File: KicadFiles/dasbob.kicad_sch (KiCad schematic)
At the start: 64 parts, among them J1 TRRS LEFT, J2 TRRS LEFT, SW1 SW_Push, SW10 SW_Push, SW11 SW_Push, SW12 SW_Push, SW13 SW_Push, SW14 SW_Push, SW15 SW_Push, SW16 SW_Push, SW17 SW_Push, SW18 SW_Push, SW19 SW_Push, SW2 SW_Push, SW20 SW_Push, SW21 SW_Push, SW22 SW_Push, SW23 SW_Push, SW24 SW_Push, SW25 SW_Push, SW26 SW_Push, SW27 SW_Push, SW28 SW_Push, SW29 SW_Push, SW3 SW_Push, SW30 SW_Push, SW31 SW_Push, SW32 SW_Push, SW33 SW_Push, SW34 SW_Push, SW35 SW_Push, SW36 SW_Push, SW4 SW_Push, SW5 SW_Push, SW6 SW_Push, SW7 SW_Push, SW8 SW_Push, SW9 SW_Push, U1 Elite-C RIGHT, U2 Elite-C LEFT, U3 OLED1, U4 OLED2

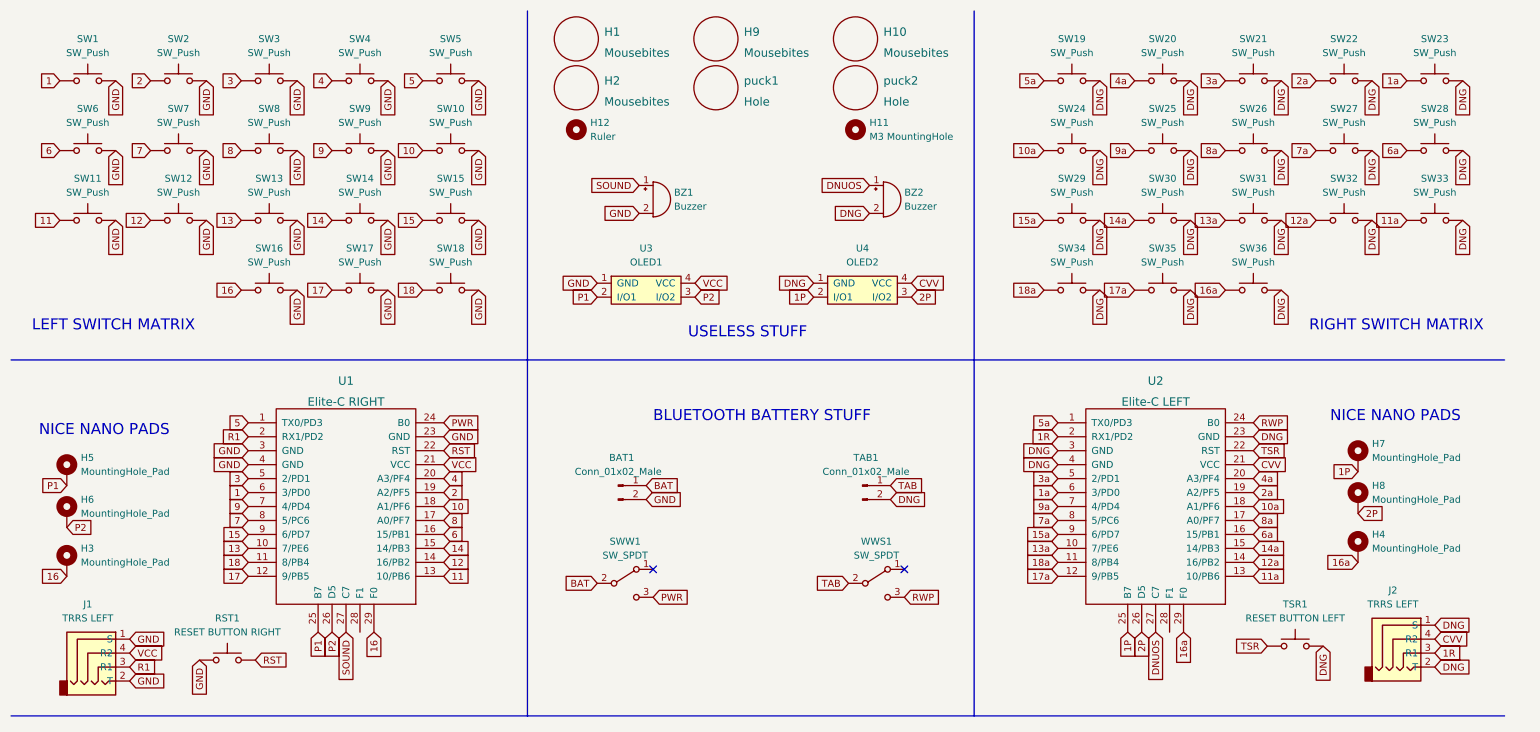
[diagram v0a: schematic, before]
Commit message: routed the oled to the wrong pins because im a ducking idiot now i fixed it
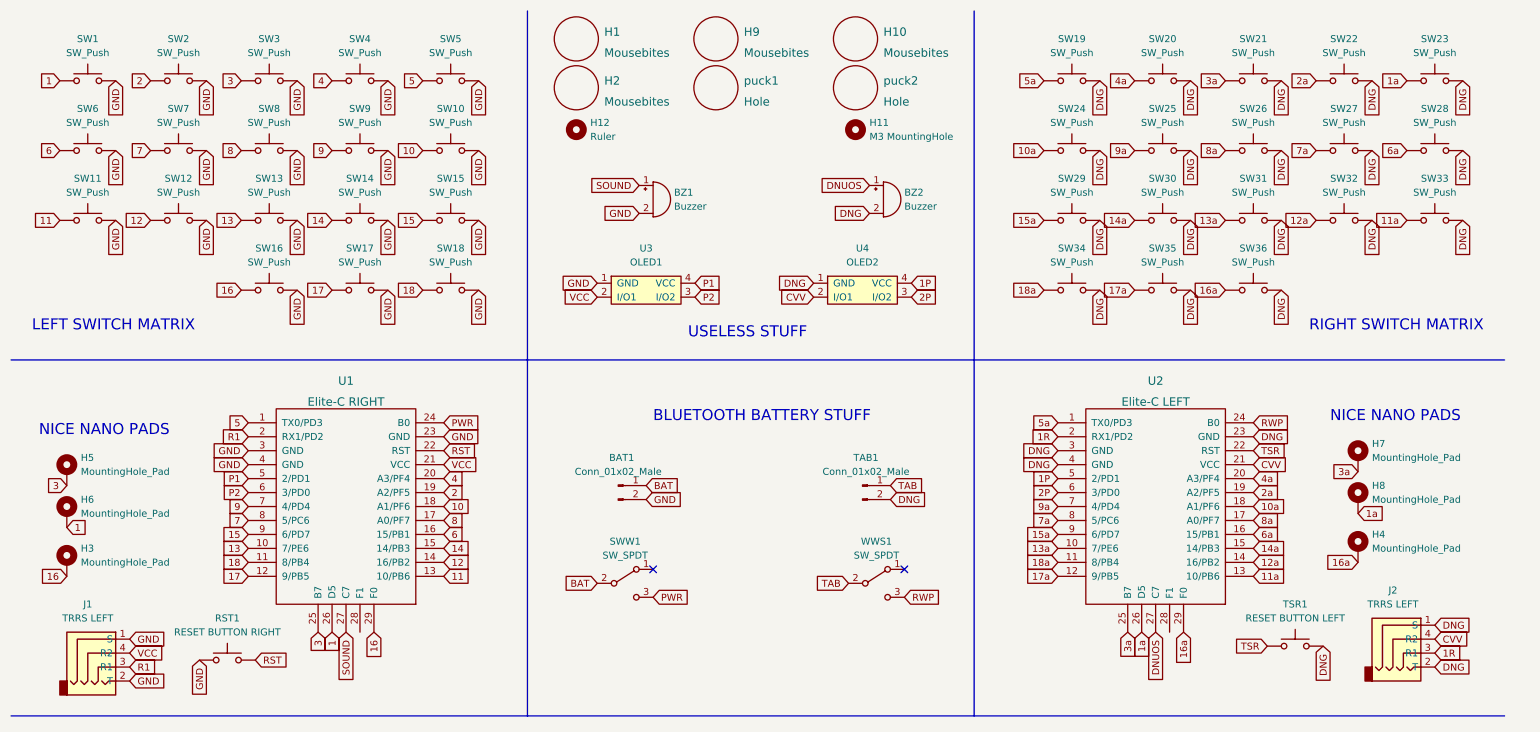
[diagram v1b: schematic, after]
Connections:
- net 1: now also H6.1, U1.26 (D5); no longer U1.6 (3/PD0)
- net 1P: now also U2.5 (2/PD1), U4.4 (VCC); no longer H7.1, U2.25 (B7), U4.2 (I/O1)
- net 1a: now also H8.1, U2.26 (D5); no longer U2.6 (3/PD0)
- net 2P: now also U2.6 (3/PD0); no longer H8.1, U2.26 (D5)
- net 3: now also H5.1, U1.25 (B7); no longer U1.5 (2/PD1)
- net 3a: now also H7.1, U2.25 (B7); no longer U2.5 (2/PD1)
- net CVV: now also U4.2 (I/O1); no longer U4.4 (VCC)
- net P1: now also U1.5 (2/PD1), U3.4 (VCC); no longer H5.1, U1.25 (B7), U3.2 (I/O1)
- net P2: now also U1.6 (3/PD0); no longer H6.1, U1.26 (D5)
- net VCC: now also U3.2 (I/O1); no longer U3.4 (VCC)
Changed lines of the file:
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@@
     )
   )
-  (global_label "1P" (shape input) (at 257.81 96.52 180) (fields_autoplaced)
-    (effects (font (size 1.27 1.27)) (justify right))
-    (property "Intersheet References" "${INTERSHEET_REFS}" (id 0) (at 252.9174 96.5994 0)
-      (effects (font (size 1.27 1.27)) (justify left) hide)
+  (global_label "3a" (shape input) (at 257.81 96.52 180) (fields_autoplaced)
+    (effects (font (size 1.27 1.27)) (justify right))
+    (property "Intersheet References" "${INTERSHEET_REFS}" (id 0) (at 253.0383 96.4406 0)
+      (effects (font (size 1.27 1.27)) (justify right) hide)
     )
   )
@@
     )
   )
-  (global_label "P1" (shape input) (at 119.38 64.77 180) (fields_autoplaced)
-    (effects (font (size 1.27 1.27)) (justify right))
-    (property "Intersheet References" "${INTERSHEET_REFS}" (id 0) (at 114.4874 64.8494 0)
+  (global_label "P1" (shape input) (at 137.16 62.23 0) (fields_autoplaced)
+    (effects (font (size 1.27 1.27)) (justify left))
+    (property "Intersheet References" "${INTERSHEET_REFS}" (id 0) (at 142.0526 62.1506 0)
       (effects (font (size 1.27 1.27)) (justify left) hide)
     )
@@
     )
   )
-  (global_label "P1" (shape input) (at 22.86 99.06 180) (fields_autoplaced)
-    (effects (font (size 1.27 1.27)) (justify right))
-    (property "Intersheet References" "${INTERSHEET_REFS}" (id 0) (at 17.9674 99.1394 0)
-      (effects (font (size 1.27 1.27)) (justify left) hide)
+  (global_label "3" (shape input) (at 22.86 99.06 180) (fields_autoplaced)
+    (effects (font (size 1.27 1.27)) (justify right))
+    (property "Intersheet References" "${INTERSHEET_REFS}" (id 0) (at 19.2374 98.9806 0)
+      (effects (font (size 1.27 1.27)) (justify right) hide)
     )
   )
@@
     )
   )
-  (global_label "3a" (shape input) (at 203.2 97.79 180) (fields_autoplaced)
-    (effects (font (size 1.27 1.27)) (justify right))
-    (property "Intersheet References" "${INTERSHEET_REFS}" (id 0) (at 198.4283 97.7106 0)
+  (global_label "3a" (shape input) (at 215.9 125.73 270) (fields_autoplaced)
+    (effects (font (size 1.27 1.27)) (justify right))
+    (property "Intersheet References" "${INTERSHEET_REFS}" (id 0) (at 215.8206 130.5017 90)
       (effects (font (size 1.27 1.27)) (justify right) hide)
     )
@@
     )
   )
-  (global_label "3" (shape input) (at 55.88 97.79 180) (fields_autoplaced)
-    (effects (font (size 1.27 1.27)) (justify right))
-    (property "Intersheet References" "${INTERSHEET_REFS}" (id 0) (at 52.2574 97.7106 0)
-      (effects (font (size 1.27 1.27)) (justify right) hide)
-    )
-  )
-  (global_label "1P" (shape input) (at 215.9 125.73 270) (fields_autoplaced)
-    (effects (font (size 1.27 1.27)) (justify right))
-    (property "Intersheet References" "${INTERSHEET_REFS}" (id 0) (at 215.8206 130.6226 90)
-      (effects (font (size 1.27 1.27)) (justify right) hide)
-    )
-  )
-  (global_label "1a" (shape input) (at 203.2 100.33 180) (fields_autoplaced)
-    (effects (font (size 1.27 1.27)) (justify right))
-    (property "Intersheet References" "${INTERSHEET_REFS}" (id 0) (at 198.4283 100.2506 0)
+  (global_label "3" (shape input) (at 68.58 125.73 270) (fields_autoplaced)
+    (effects (font (size 1.27 1.27)) (justify right))
+    (property "Intersheet References" "${INTERSHEET_REFS}" (id 0) (at 68.5006 129.3526 90)
+      (effects (font (size 1.27 1.27)) (justify right) hide)
+    )
+  )
+  (global_label "1P" (shape input) (at 203.2 97.79 180) (fields_autoplaced)
+    (effects (font (size 1.27 1.27)) (justify right))
+    (property "Intersheet References" "${INTERSHEET_REFS}" (id 0) (at 198.3074 97.7106 0)
+      (effects (font (size 1.27 1.27)) (justify right) hide)
+    )
+  )
+  (global_label "1a" (shape input) (at 218.44 125.73 270) (fields_autoplaced)
+    (effects (font (size 1.27 1.27)) (justify right))
+    (property "Intersheet References" "${INTERSHEET_REFS}" (id 0) (at 218.3606 130.5017 90)
       (effects (font (size 1.27 1.27)) (justify right) hide)
     )
@@
     )
   )
-  (global_label "1P" (shape input) (at 158.75 64.77 180) (fields_autoplaced)
-    (effects (font (size 1.27 1.27)) (justify right))
-    (property "Intersheet References" "${INTERSHEET_REFS}" (id 0) (at 153.8574 64.8494 0)
+  (global_label "1P" (shape input) (at 176.53 62.23 0) (fields_autoplaced)
+    (effects (font (size 1.27 1.27)) (justify left))
+    (property "Intersheet References" "${INTERSHEET_REFS}" (id 0) (at 181.4226 62.1506 0)
       (effects (font (size 1.27 1.27)) (justify left) hide)
     )
@@
     )
   )
-  (global_label "VCC" (shape input) (at 137.16 62.23 0) (fields_autoplaced)
-    (effects (font (size 1.27 1.27)) (justify left))
-    (property "Intersheet References" "${INTERSHEET_REFS}" (id 0) (at 143.2017 62.1506 0)
+  (global_label "VCC" (shape input) (at 119.38 64.77 180) (fields_autoplaced)
+    (effects (font (size 1.27 1.27)) (justify right))
+    (property "Intersheet References" "${INTERSHEET_REFS}" (id 0) (at 113.3383 64.8494 0)
       (effects (font (size 1.27 1.27)) (justify left) hide)
     )
@@
     )
   )
-  (global_label "P2" (shape input) (at 22.86 106.68 0) (fields_autoplaced)
-    (effects (font (size 1.27 1.27)) (justify left))
-    (property "Intersheet References" "${INTERSHEET_REFS}" (id 0) (at 27.7526 106.6006 0)
+  (global_label "1" (shape input) (at 22.86 106.68 0) (fields_autoplaced)
+    (effects (font (size 1.27 1.27)) (justify left))
+    (property "Intersheet References" "${INTERSHEET_REFS}" (id 0) (at 26.4826 106.6006 0)
       (effects (font (size 1.27 1.27)) (justify left) hide)
     )
@@
     )
   )
-  (global_label "P2" (shape input) (at 71.12 125.73 270) (fields_autoplaced)
-    (effects (font (size 1.27 1.27)) (justify right))
-    (property "Intersheet References" "${INTERSHEET_REFS}" (id 0) (at 71.1994 130.6226 90)
+  (global_label "P2" (shape input) (at 55.88 100.33 180) (fields_autoplaced)
+    (effects (font (size 1.27 1.27)) (justify right))
+    (property "Intersheet References" "${INTERSHEET_REFS}" (id 0) (at 50.9874 100.4094 0)
       (effects (font (size 1.27 1.27)) (justify left) hide)
     )
@@
     )
   )
-  (global_label "2P" (shape input) (at 218.44 125.73 270) (fields_autoplaced)
-    (effects (font (size 1.27 1.27)) (justify right))
-    (property "Intersheet References" "${INTERSHEET_REFS}" (id 0) (at 218.3606 130.6226 90)
+  (global_label "2P" (shape input) (at 203.2 100.33 180) (fields_autoplaced)
+    (effects (font (size 1.27 1.27)) (justify right))
+    (property "Intersheet References" "${INTERSHEET_REFS}" (id 0) (at 198.3074 100.2506 0)
       (effects (font (size 1.27 1.27)) (justify right) hide)
     )
@@
     )
   )
-  (global_label "CVV" (shape input) (at 176.53 62.23 0) (fields_autoplaced)
-    (effects (font (size 1.27 1.27)) (justify left))
-    (property "Intersheet References" "${INTERSHEET_REFS}" (id 0) (at 182.3902 62.1506 0)
+  (global_label "CVV" (shape input) (at 158.75 64.77 180) (fields_autoplaced)
+    (effects (font (size 1.27 1.27)) (justify right))
+    (property "Intersheet References" "${INTERSHEET_REFS}" (id 0) (at 152.8898 64.8494 0)
       (effects (font (size 1.27 1.27)) (justify left) hide)
     )
@@
     )
   )
-  (global_label "P1" (shape input) (at 68.58 125.73 270) (fields_autoplaced)
-    (effects (font (size 1.27 1.27)) (justify right))
-    (property "Intersheet References" "${INTERSHEET_REFS}" (id 0) (at 68.6594 130.6226 90)
-      (effects (font (size 1.27 1.27)) (justify left) hide)
-    )
-  )
-  (global_label "1" (shape input) (at 55.88 100.33 180) (fields_autoplaced)
-    (effects (font (size 1.27 1.27)) (justify right))
-    (property "Intersheet References" "${INTERSHEET_REFS}" (id 0) (at 52.2574 100.2506 0)
+  (global_label "P1" (shape input) (at 55.88 97.79 180) (fields_autoplaced)
+    (effects (font (size 1.27 1.27)) (justify right))
+    (property "Intersheet References" "${INTERSHEET_REFS}" (id 0) (at 50.9874 97.8694 0)
+      (effects (font (size 1.27 1.27)) (justify left) hide)
+    )
+  )
+  (global_label "1" (shape input) (at 71.12 125.73 270) (fields_autoplaced)
+    (effects (font (size 1.27 1.27)) (justify right))
+    (property "Intersheet References" "${INTERSHEET_REFS}" (id 0) (at 71.0406 129.3526 90)
       (effects (font (size 1.27 1.27)) (justify right) hide)
     )
@@
     )
   )
-  (global_label "2P" (shape input) (at 257.81 104.14 0) (fields_autoplaced)
-    (effects (font (size 1.27 1.27)) (justify left))
-    (property "Intersheet References" "${INTERSHEET_REFS}" (id 0) (at 262.7026 104.0606 0)
-      (effects (font (size 1.27 1.27)) (justify left) hide)
-    )
+  (global_label "1a" (shape input) (at 257.81 104.14 0) (fields_autoplaced)
+    (effects (font (size 1.27 1.27)) (justify left))
+    (property "Intersheet References" "${INTERSHEET_REFS}" (id 0) (at 262.5817 104.0606 0)
+      (effects (font (size 1.27 1.27)) (justify left) hide)
+    )

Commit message: buzzer was not working
buzzer was not working put a jumper for it on the board
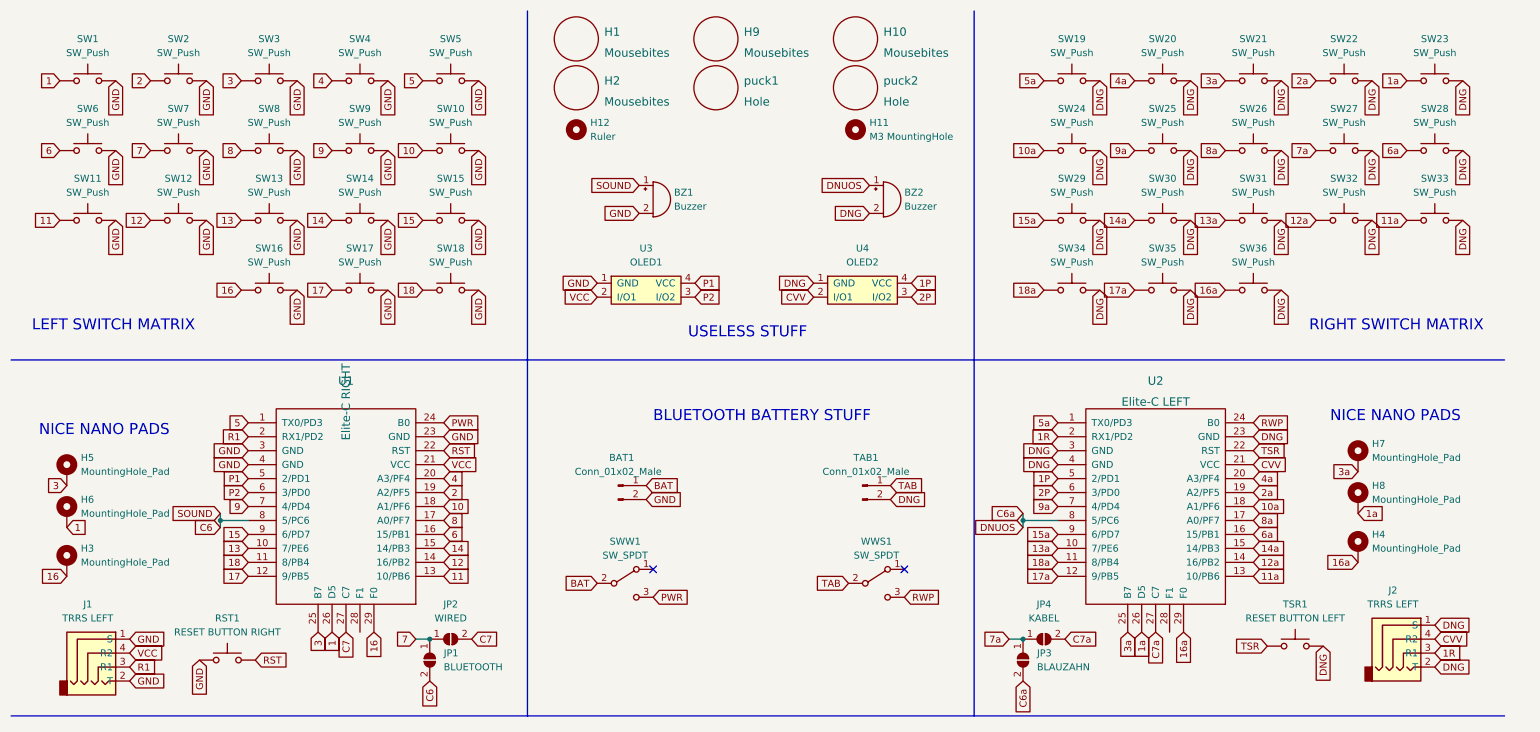
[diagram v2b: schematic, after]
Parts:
- added JP1: BLUETOOTH, keebio:JUMPER_SMD_2DUB, symbol Jumper:SolderJumper_2_Open
- added JP2: WIRED, keebio:JUMPER_SMD_2DUB, symbol Jumper:SolderJumper_2_Open
- added JP3: BLAUZAHN, keebio:JUMPER_SMD_2DUB, symbol Jumper:SolderJumper_2_Open
- added JP4: KABEL, keebio:JUMPER_SMD_2DUB, symbol Jumper:SolderJumper_2_Open
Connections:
- net 7: now also JP1.1 (A), JP2.1 (A); no longer U1.8 (5/PC6)
- net 7a: now also JP3.1 (A), JP4.1 (A); no longer U2.8 (5/PC6)
- net DNUOS renamed C6a
- net C6a: now also U2.8 (5/PC6), JP3.2 (B); no longer U2.27 (C7)
- net SOUND renamed C6
- net C6: now also U1.8 (5/PC6), JP1.2 (B); no longer U1.27 (C7)
- new net C7: JP2.2 (B), U1.27 (C7)
- new net C7a: JP4.2 (B), U2.27 (C7)
